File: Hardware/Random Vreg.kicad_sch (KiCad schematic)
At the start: 11 parts, among them J1 Conn_01x07_Male, J2 Conn_01x04_Male, J3 Conn_01x02_Male, J4 Conn_01x02_Male, J5 Conn_01x02_Male, J6 Conn_01x02_Male, J7 Conn_01x08_Male, J9 QWIIC_Stackable, U1 R1501J033B-T1-JE

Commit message: ...
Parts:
- added C?: 1.0uF, Capacitor_SMD:C_0603_1608Metric, symbol Device:C
- added C?: 22uf, Tinker:CP_EIA-6032-28-Tantalumm_HandSolder, symbol Device:CP
- added J10: Conn_01x02_Male, Tinker:Board_Stacker_2, symbol Connector:Conn_01x02_Male
- added U?: R1501J033B-T1-JE, Tinker:R1501J033BT1JE, symbol R1501J033B-T1-JE:R1501J033B-T1-JE
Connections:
- net ATTACH is gone; now on net RESET: J7.2 (Pin_2)
- net GND: now also C?.2, C?.2, J10.2 (Pin_2), U?.2 (GND_1), U?.3 (GND_2), U?.6 (GND_3)
- net RESET: no longer J7.1 (Pin_1)
- net SCL: no longer J7.3 (Pin_3)
- net SDA: no longer J7.5 (Pin_5)
- net Vout: now also C?.1, U?.1 (VDD), U?.4 (CE)
- net ALERT renamed ~{SCS}0
- net GPIO renamed MOSI
- net POWER_OK2 renamed SCLK
- net POWER_OK3 renamed MISO
- new net: C?.1, J10.1 (Pin_1), U?.5 (VOUT)
- new net ~{RESET}: J7.1 (Pin_1)
- new net ~{SCS}1: J7.5 (Pin_5)
- new net ~{SCS}2: J7.3 (Pin_3)
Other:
- note added: "SPI"
- note added: "Vrnd (Pick a voltage)"
- note added: "Vsec (3v3)"
- note removed: "Control"
- moved on the sheet: C1, C2, U1

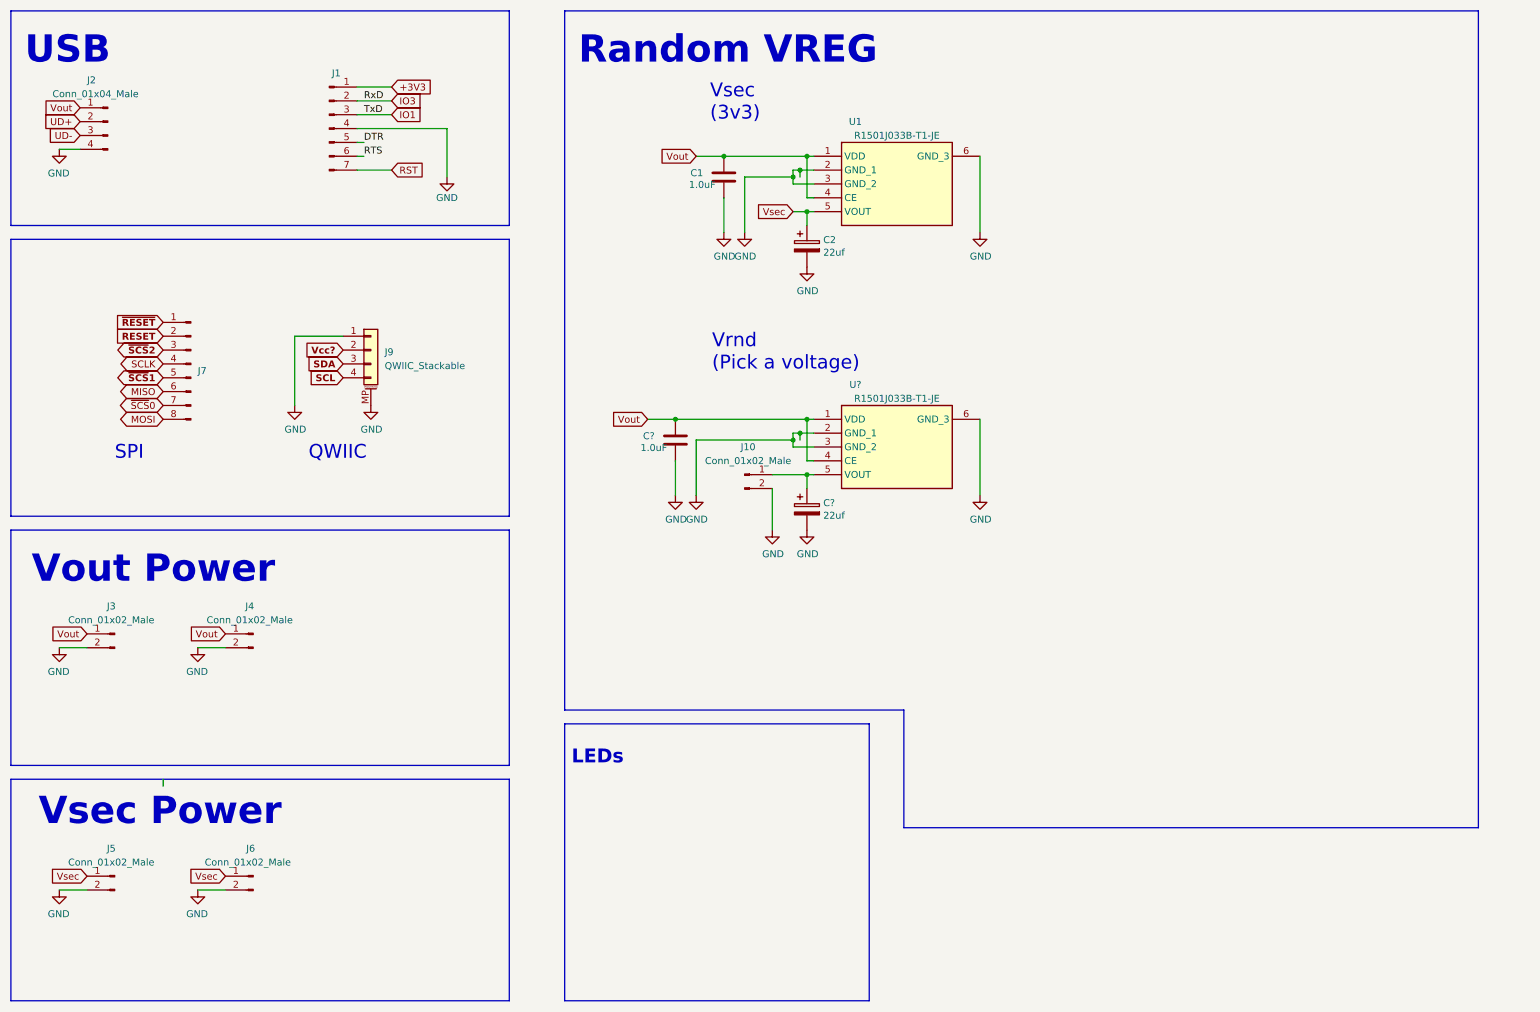
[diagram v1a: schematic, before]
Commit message: Re-doing Random VREG
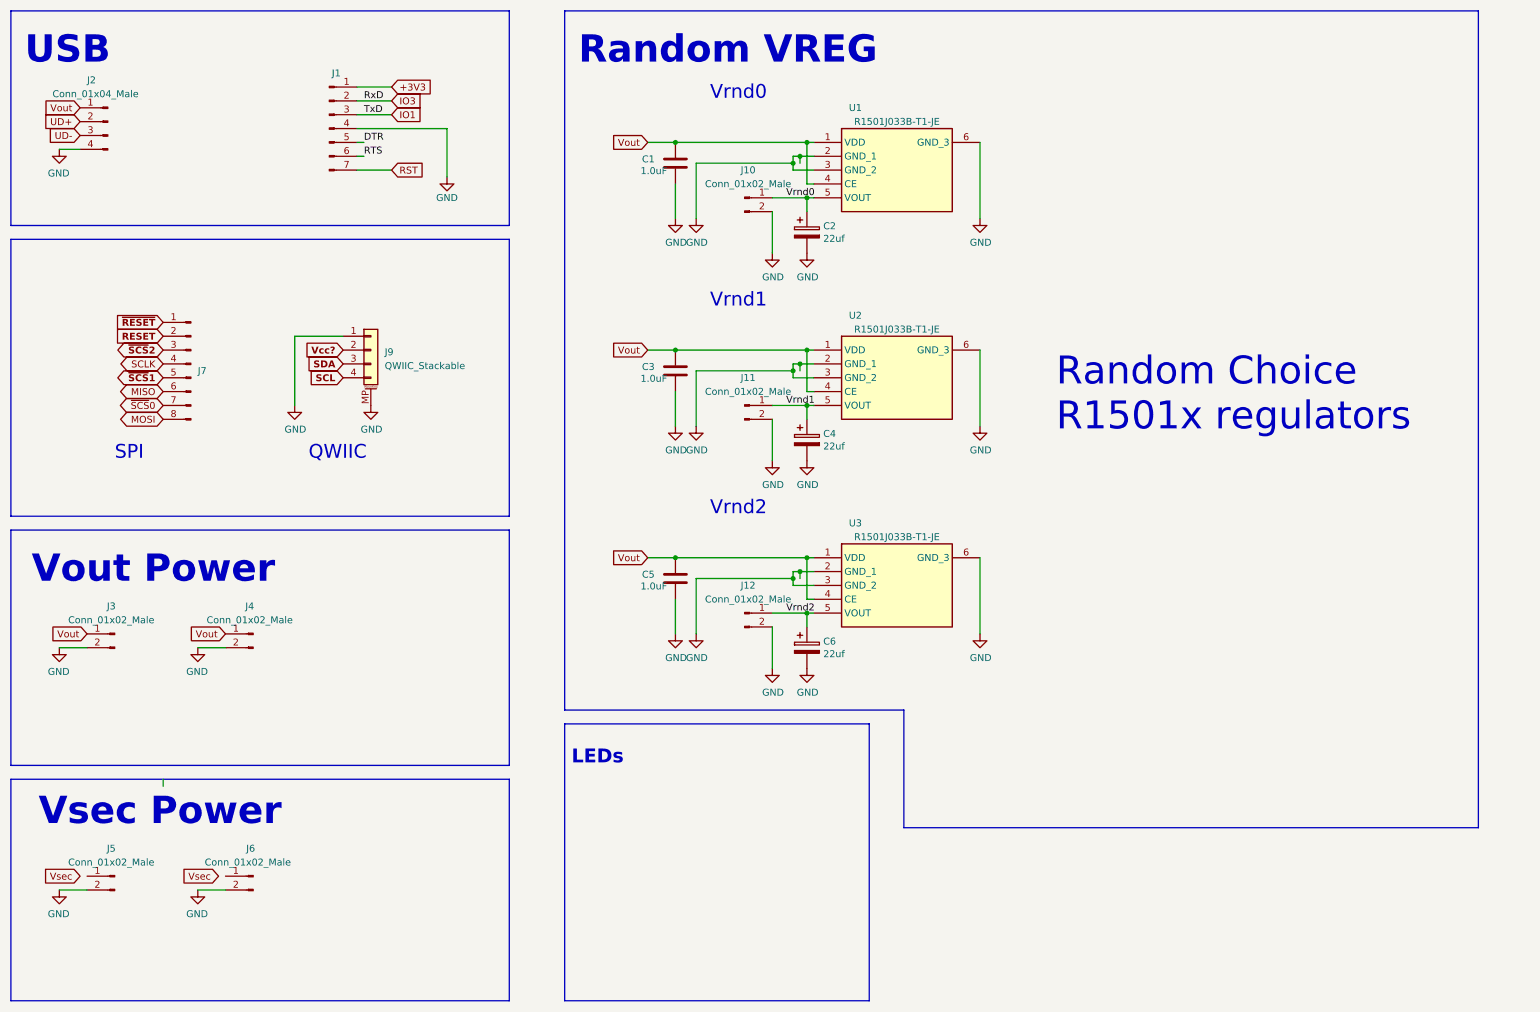
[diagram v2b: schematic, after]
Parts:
- added C5: 1.0uF, Capacitor_SMD:C_0603_1608Metric, symbol Device:C
- added C6: 22uf, Tinker:CP_EIA-6032-28-Tantalumm_HandSolder, symbol Device:CP
- added J10, J12: Conn_01x02_Male, Tinker:Board_Stacker_2, symbol Connector:Conn_01x02_Male
- added U3: R1501J033B-T1-JE, Tinker:R1501J033BT1JE, symbol R1501J033B-T1-JE:R1501J033B-T1-JE
- gave numbers to parts that had none: 3
- renumbered J10 to J11
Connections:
- net GND: now also C5.2, C6.2, J10.2 (Pin_2), J12.2 (Pin_2), U3.2 (GND_1), U3.3 (GND_2), U3.6 (GND_3)
- net Vout: now also C5.1, U3.1 (VDD), U3.4 (CE)
- net Vsec: no longer C2.1, J5.1 (Pin_1), J6.1 (Pin_1), U1.5 (VOUT)
- net Vrnd1: now reaches C4.1, J11.1 (Pin_1), U2.5 (VOUT)
- new net Vrnd0: C2.1, J10.1 (Pin_1), U1.5 (VOUT)
- new net Vrnd2: C6.1, J12.1 (Pin_1), U3.5 (VOUT)
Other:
- note added: "Random Choice R1501x regulators"
- note added: "Vrnd0"
- note added: "Vrnd1"
- note added: "Vrnd2"
- note removed: "Vrnd (Pick a voltage)"
- note removed: "Vsec (3v3)"
- moved on the sheet: C1, C2, C3, C4, J11, U1, U2

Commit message: Random VREG!
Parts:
- added C7: 100nf, Capacitor_SMD:C_0603_1608Metric, symbol Device:C
- added R1, R2, R3, R4, R5, R6, R7: 10K, Resistor_SMD:R_0603_1608Metric, symbol Device:R
- added U4: PCA9557BS, Package_DFN_QFN:HVQFN-16-1EP_3x3mm_P0.5mm_EP1.5x1.5mm, symbol Interface_Expansion:PCA9557BS
- renumbered C5 to C1, C3 to C2, C1 to C3, C6 to C4, C4 to C5, C2 to C6, J12 to J10, J10 to J12, U3 to U1, U1 to U3
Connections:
- net GND: now also C7.2, R2.2, R3.2, R4.2, R5.2, R6.2, R7.2, U4.6 (VSS)
- net SCL: now also U4.15 (SCL)
- net SDA: now also U4.16 (SDA)
- net Vcc?: now also C7.1, R1.1, U4.14 (VDD)
- net Vout: no longer U1.4 (CE), U2.4 (CE), U3.4 (CE)
- new net: R1.2, U4.13 (~{RESET})
- new net A0: R5.1, U4.1 (A0)
- new net A1: R6.1, U4.2 (A1)
- new net A2: R7.1, U4.3 (A2)
- new net CE0: R2.1, U1.4 (CE), U4.4 (IO0)
- new net CE1: R3.1, U2.4 (CE), U4.5 (IO1)
- new net CE2: R4.1, U3.4 (CE), U4.7 (IO2)
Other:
- moved on the sheet: C1, C3, C4, C6, J10, J12, U1, U2, U3
